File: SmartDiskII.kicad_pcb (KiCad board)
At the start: 2 copper layers, 100 x 77.5 mm, 43 parts, among them J1 Apple II Expansion Slot, J2 DRV, U1 74LS174, U10 27C256, U11 74LS245, U12 74LS323, U13 74LS00, U14 74LS174, U2 NE556, U3 74LS05, U4 74LS132, U5 74LS259/9334, U6 74LS20, U7 74LS21, U8 2758/16/32 P6, U9 74LS30

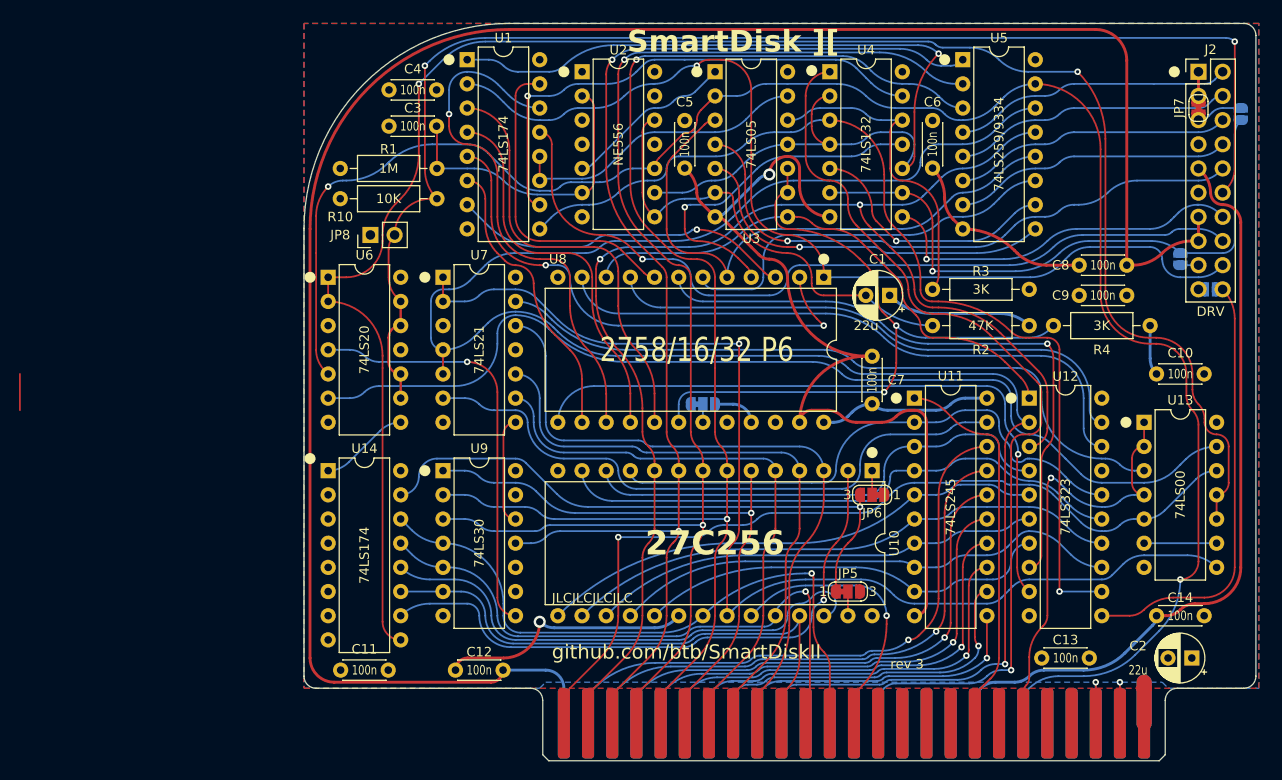
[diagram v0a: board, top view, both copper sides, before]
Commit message: readd second floppy connector
reference number changes
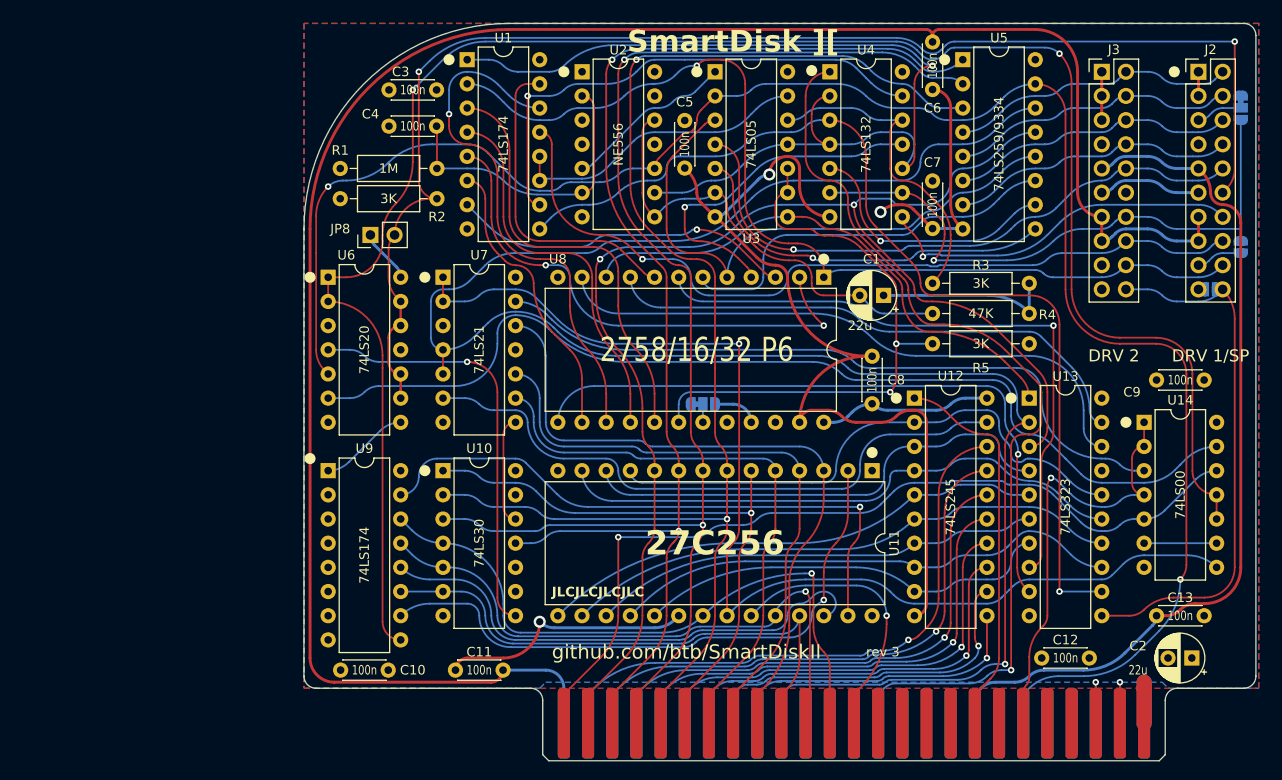
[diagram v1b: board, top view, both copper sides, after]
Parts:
- removed the C9 at (192.6, 92.1)
- removed JP5, JP6: ~, Jumper:SolderJumper-3_P1.3mm_Bridged12_RoundedPad1.0x1.5mm_NumberLabels
- removed JP7: ~, Jumper:SolderJumper-2_P1.3mm_Bridged_RoundedPad1.0x1.5mm
- added J3: DRV 2, MyConnector:PinHeader_2x10_P2.54mm_Vertical_Shrouded, F.Cu at (194.9, 68.6)
- J2: value DRV -> DRV 1/SP
- JP1: footprint Jumper:SolderJumper-2_P1.3mm_Open_RoundedPad1.0x1.5mm -> Jumper:SolderJumper-3_P1.3mm_Bridged12_RoundedPad1.0x1.5mm_NumberLabels
- R2: renamed from R10; value 10K -> 3K
- moved C6 31.1 mm to (177.2, 65.4), turned to -90 degrees
- moved R5 12.8 mm to (187.3, 97.2)
- moved JP2 6.48 mm to (209.6, 87.0)
- moved C7 6.35 mm to (177.2, 80.0)
- moved R4 1.27 mm to (177.2, 94.0)
- moved JP1 0.67 mm to (209.6, 72.4), turned to -90 degrees
- moved C9 0.64 mm to (200.7, 101.0)
- moved C1 0.63 mm to (172.0, 92.1)
- moved R3 0.63 mm to (187.3, 90.8)
- renumbered C11 to C10, C12 to C11, C13 to C12, C14 to C13, C4 to C3, C3 to C4, C8 to C6, C6 to C7, C7 to C8, C10 to C9, R2 to R4, R4 to R5, U9 to U10, U10 to U11, U11 to U12, U12 to U13, U13 to U14, U14 to U9
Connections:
- J2 pad 7: /~{EN3.5} -> unconnected-(J2-Pin_7-Pad7)
- JP1 pad 1: /~{ENBL 2} -> GND
- U11 pad 1: Net-(JP6-C) -> +5V
- U11 pad 27: Net-(JP5-C) -> Net-(U11-A14)
- U9 pad 15: Net-(JP5-A) -> Net-(U11-A14)
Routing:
- net Net-(U11-A14): track 0.00 -> 63.8 mm, vias 0 -> 1
- net Net-(JP5-A): track 63.0 -> 0.00 mm, vias 1 -> 0
- net +5V: track 48.0 -> 62.7 mm
- net Net-(U8-~{CE}): track 73.1 -> 61.3 mm
- net /W PROT: track 45.7 -> 56.5 mm
- net -12V: track 80.3 -> 91.2 mm
- net GND: track 150.6 -> 160.9 mm, vias 2 -> 3
- net +12V: track 209.4 -> 205.8 mm
- net Net-(J2-Pin_17): track 1.91 -> 4.83 mm
- net Net-(JP6-C): track 2.54 -> 0.00 mm
- net Net-(JP5-C): track 2.54 -> 0.00 mm
- net /ENCOMMON: track 194.3 -> 196.5 mm
- net /SEL: track 145.9 -> 143.7 mm
- net Net-(U1-Cp): track 103.0 -> 104.9 mm
- net Net-(U13-Q0): track 65.8 -> 67.7 mm
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
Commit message: Protect pin 12 with Diode
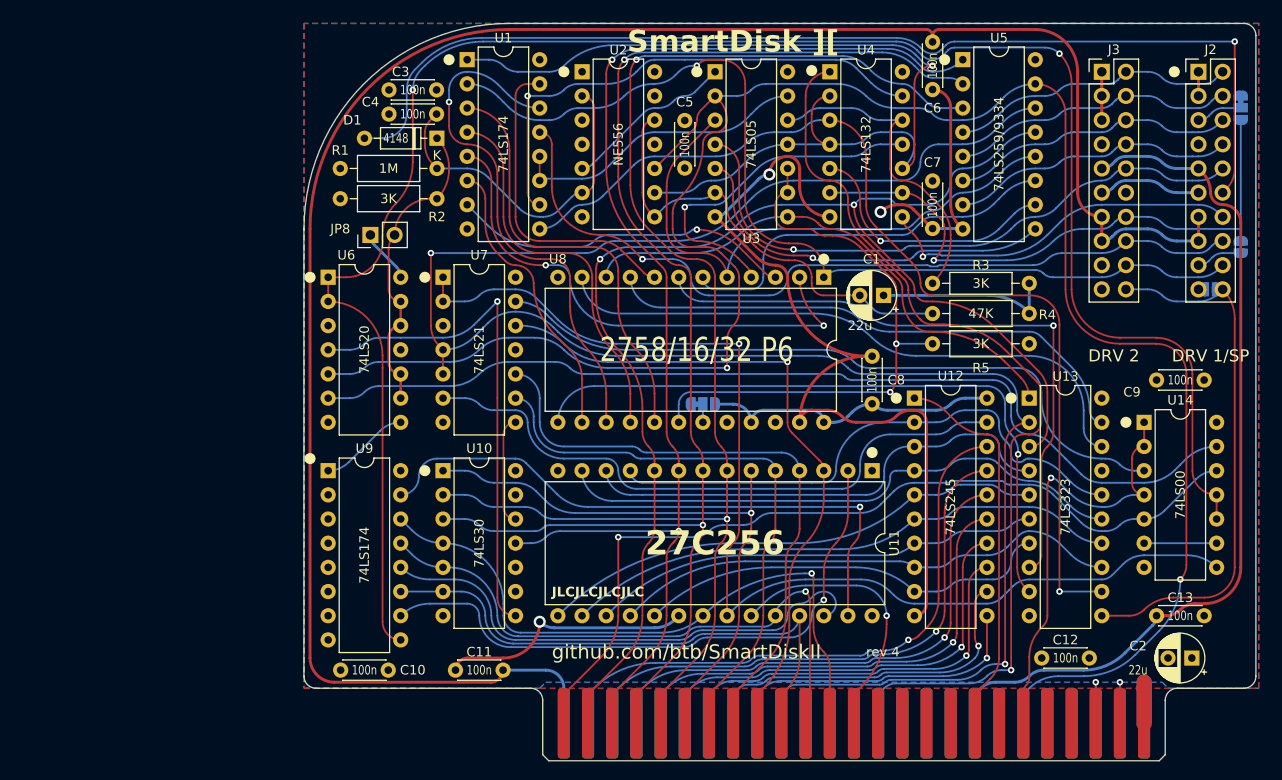
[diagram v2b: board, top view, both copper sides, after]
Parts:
- added D1: 4148, Diode_THT:D_DO-35_SOD27_P7.62mm_Horizontal, F.Cu at (125.1, 75.6)
- moved C4 1.27 mm to (125.1, 73.0)
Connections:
- JP8 pad 2: /SEL -> Net-(D1-K)
- R2 pad 1: /SEL -> Net-(D1-K)
- U6 pad 10: /SEL -> Net-(D1-K)
- U6 pad 12: /SEL -> Net-(D1-K)
- U6 pad 13: /SEL -> Net-(D1-K)
- U6 pad 9: /SEL -> Net-(D1-K)
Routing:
- net Net-(D1-K): track 0.00 -> 32.8 mm
- net /SEL: track 143.7 -> 114.9 mm, vias 2 -> 1
- net /~{RES}: track 192.3 -> 213.5 mm
- net /~{HISTROBE}: track 44.3 -> 53.5 mm
- net +5V: track 62.7 -> 71.7 mm
- net GND: track 160.9 -> 154.7 mm
- net /CLRCOMMON: track 106.7 -> 101.6 mm
- net Net-(U2A-THR): track 31.9 -> 36.0 mm
- net /~{DEVSEL}: track 201.0 -> 203.9 mm, vias 1 -> 2
- net /A7: track 71.9 -> 70.7 mm, vias 0 -> 1

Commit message: tweaks
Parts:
- moved U10 1.27 mm to (125.7, 111.8)
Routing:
- net /~{RES}: track 213.5 -> 215.9 mm
- net Net-(U11-A12): track 63.8 -> 61.9 mm
- net Net-(U11-A14): track 63.8 -> 62.0 mm
- net Net-(U10-Pad12): track 11.5 -> 12.8 mm
- net /~{HISTROBE}: track 53.5 -> 54.8 mm
- net /A8: track 57.9 -> 56.6 mm
- net Net-(U11-A13): track 54.1 -> 53.1 mm
- net /A9: track 63.4 -> 62.6 mm
- net /WR REQ: track 63.6 -> 62.8 mm
- net Net-(U5-Q4): track 40.1 -> 39.3 mm
- net /A10: track 67.4 -> 66.7 mm
- net +5V: track 71.7 -> 72.2 mm

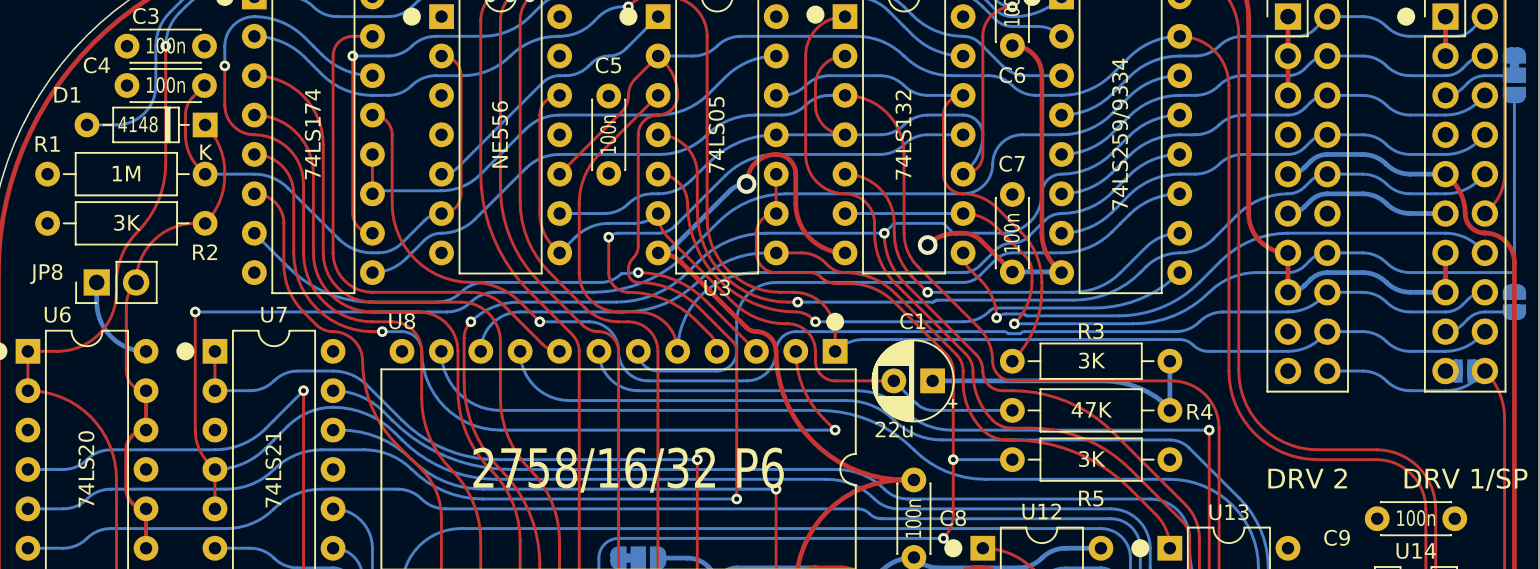
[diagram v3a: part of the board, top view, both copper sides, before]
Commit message: use 3.3k instead of 3k. gnd jumper for drv pin 7
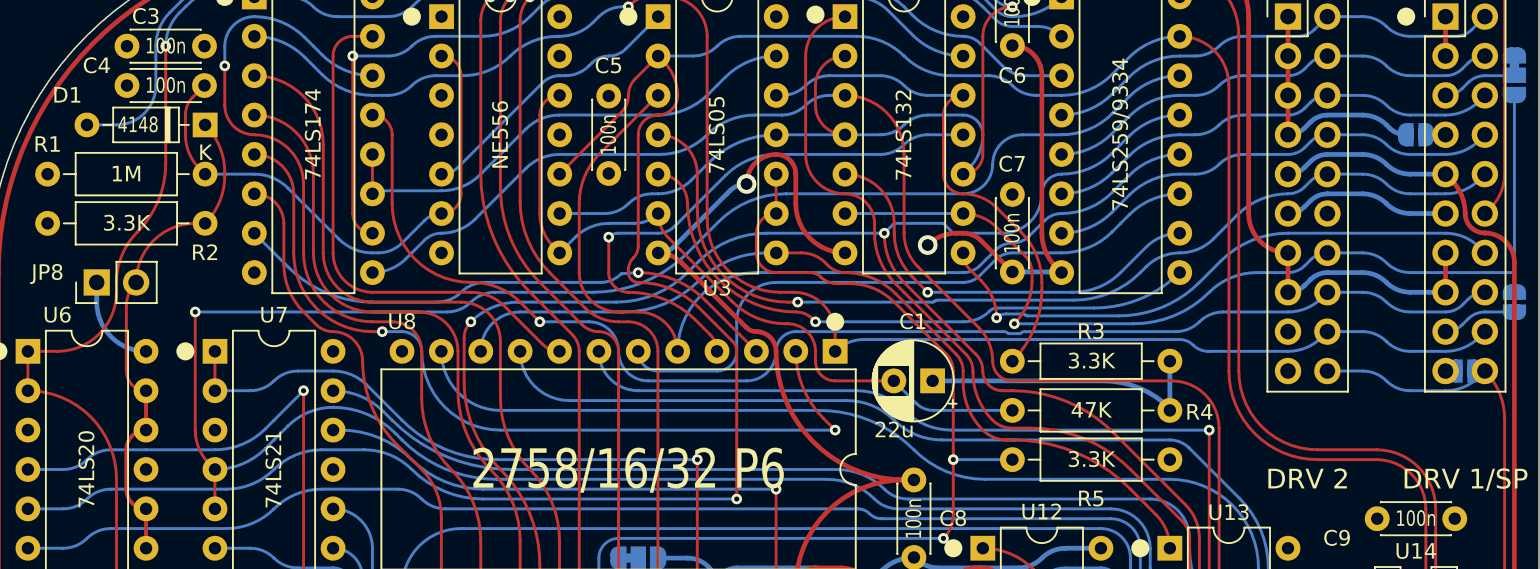
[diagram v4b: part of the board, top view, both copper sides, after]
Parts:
- added JP5: ~, Jumper:SolderJumper-2_P1.3mm_Open_RoundedPad1.0x1.5mm, B.Cu at (203.2, 76.2)
- R2, R3, R5: value 3K -> 3.3K
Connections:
- J2 pad 7: unconnected-(J2-Pin_7-Pad7) -> Net-(J2-Pin_7)
- J3 pad 7: unconnected-(J3-Pin_7-Pad7) -> GND
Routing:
- net GND: track 154.7 -> 165.5 mm
- net Net-(J2-Pin_7): track 0.00 -> 1.25 mm

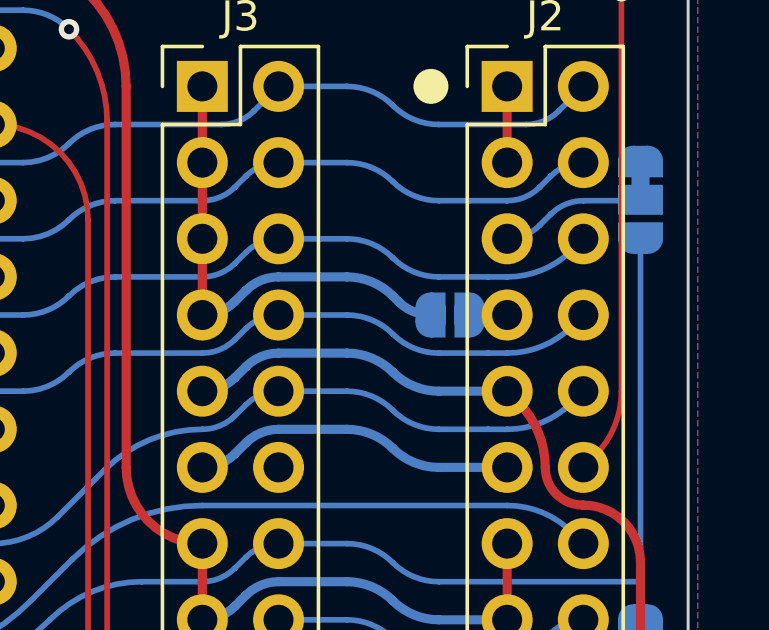
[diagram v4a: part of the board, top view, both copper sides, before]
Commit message: ground drive pin 7 by default
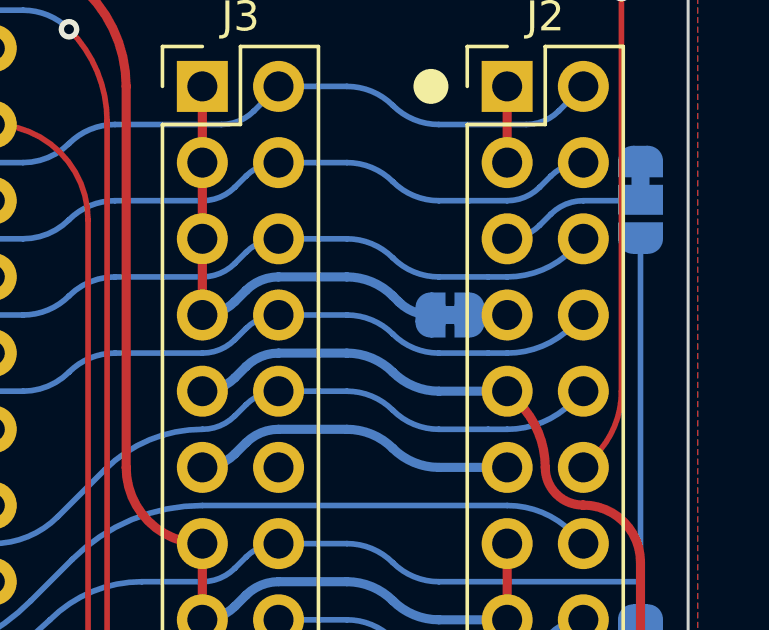
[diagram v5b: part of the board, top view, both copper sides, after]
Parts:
- JP5: footprint Jumper:SolderJumper-2_P1.3mm_Open_RoundedPad1.0x1.5mm -> Jumper:SolderJumper-2_P1.3mm_Bridged_RoundedPad1.0x1.5mm
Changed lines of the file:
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@@
       ))
   )
-  (footprint "Jumper:SolderJumper-2_P1.3mm_Open_RoundedPad1.0x1.5mm" (layer "B.Cu")
+  (footprint "Jumper:SolderJumper-2_P1.3mm_Bridged_RoundedPad1.0x1.5mm" (layer "B.Cu")
     (at 203.2 76.2)
-    (descr "SMD Solder Jumper, 1x1.5mm, rounded Pads, 0.3mm gap, open")
-    (tags "solder jumper open")
+    (descr "SMD Solder Jumper, 1x1.5mm, rounded Pads, 0.3mm gap, bridged with 1 copper strip")
+    (tags "net tie solder jumper bridged")
     (property "Sheetfile" "SmartDiskII.kicad_sch")
     (property "Sheetname" "")
-    (property "ki_description" "Solder Jumper, 2-pole, open")
+    (property "ki_description" "Solder Jumper, 2-pole, closed/bridged")
     (property "ki_keywords" "solder jumper SPST")
     (attr exclude_from_pos_files)
-    (fp_text reference "JP5" (at 0 -1.905) (layer "B.SilkS")
+    (net_tie_pad_groups "1, 2")
+    (fp_text reference "JP5" (at 0 1.8 180) (layer "B.SilkS")
         (effects (font (size 1 1) (thickness 0.15)) (justify mirror))
     )
-    (fp_text value "~" (at 0 -1.9) (layer "B.Fab")
+    (fp_text value "~" (at 0 -1.9 180) (layer "B.Fab")
         (effects (font (size 1 1) (thickness 0.15)) (justify mirror))
     )
+    (fp_poly
+      (pts
+        (xy 0.25 0.3)
+        (xy -0.25 0.3)
+        (xy -0.25 -0.3)
+        (xy 0.25 -0.3)
+      )
+      (stroke (width 0) (type solid)) (fill solid) (layer "B.Cu"))
     (fp_line (start -1.4 -0.3) (end -1.4 0.3)
       (stroke (width 0.12) (type solid)) (layer "B.SilkS"))
